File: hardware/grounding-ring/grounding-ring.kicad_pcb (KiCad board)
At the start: 2 copper layers, 26 x 34.4 mm, 2 parts, among them P1 CONN_1

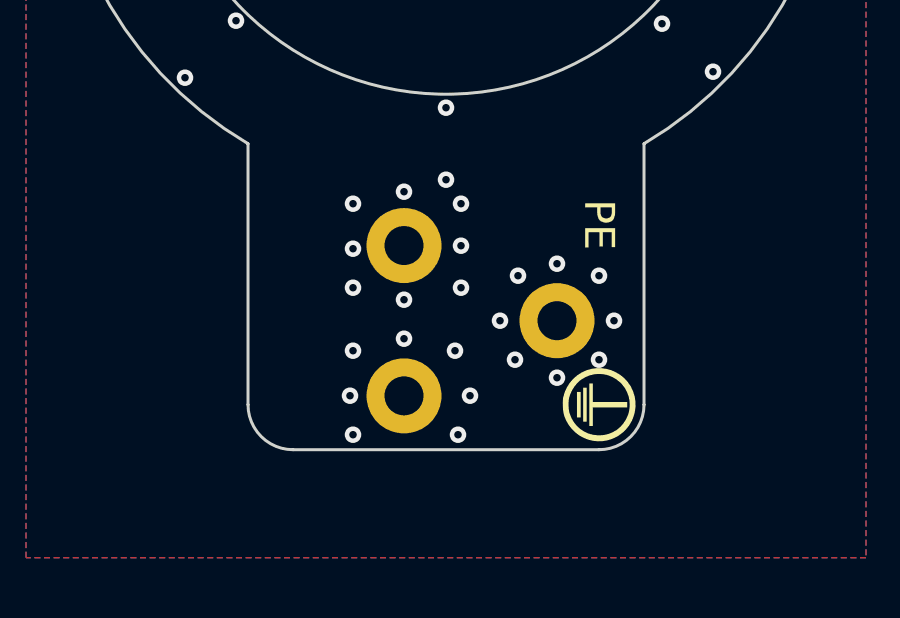
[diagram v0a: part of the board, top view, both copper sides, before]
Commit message: added warp3 bohrschablone
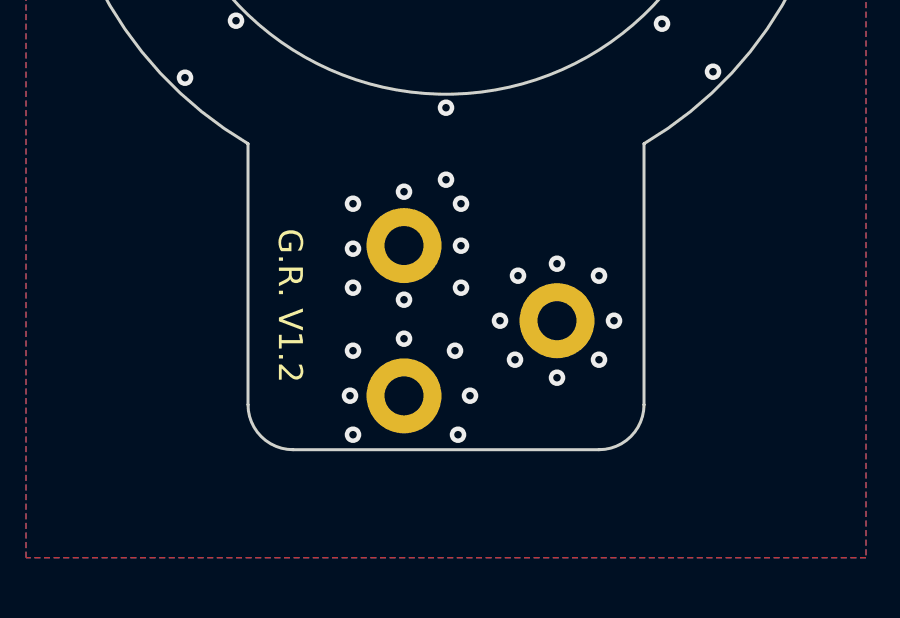
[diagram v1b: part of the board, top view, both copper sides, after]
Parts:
- G***: moved to B.Cu
- P1: value CONN_1 -> 36-4908-ND; moved to B.Cu
- turned P1 to -90 degrees
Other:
- board text added: "G.R. V1.2"
- board text removed: "G.R. 1.1"
